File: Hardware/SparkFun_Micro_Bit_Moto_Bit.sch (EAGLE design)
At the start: 47 parts, among them J1 5.5x2.1mm Barrel, J2 CORTEX_DEBUGPTH, J6 1X04_SMD_STRAIGHT_COMBO, U1 CY8C4245LQI-483, U2 TPS62172, U3 micro:bit, U4 DRV8835

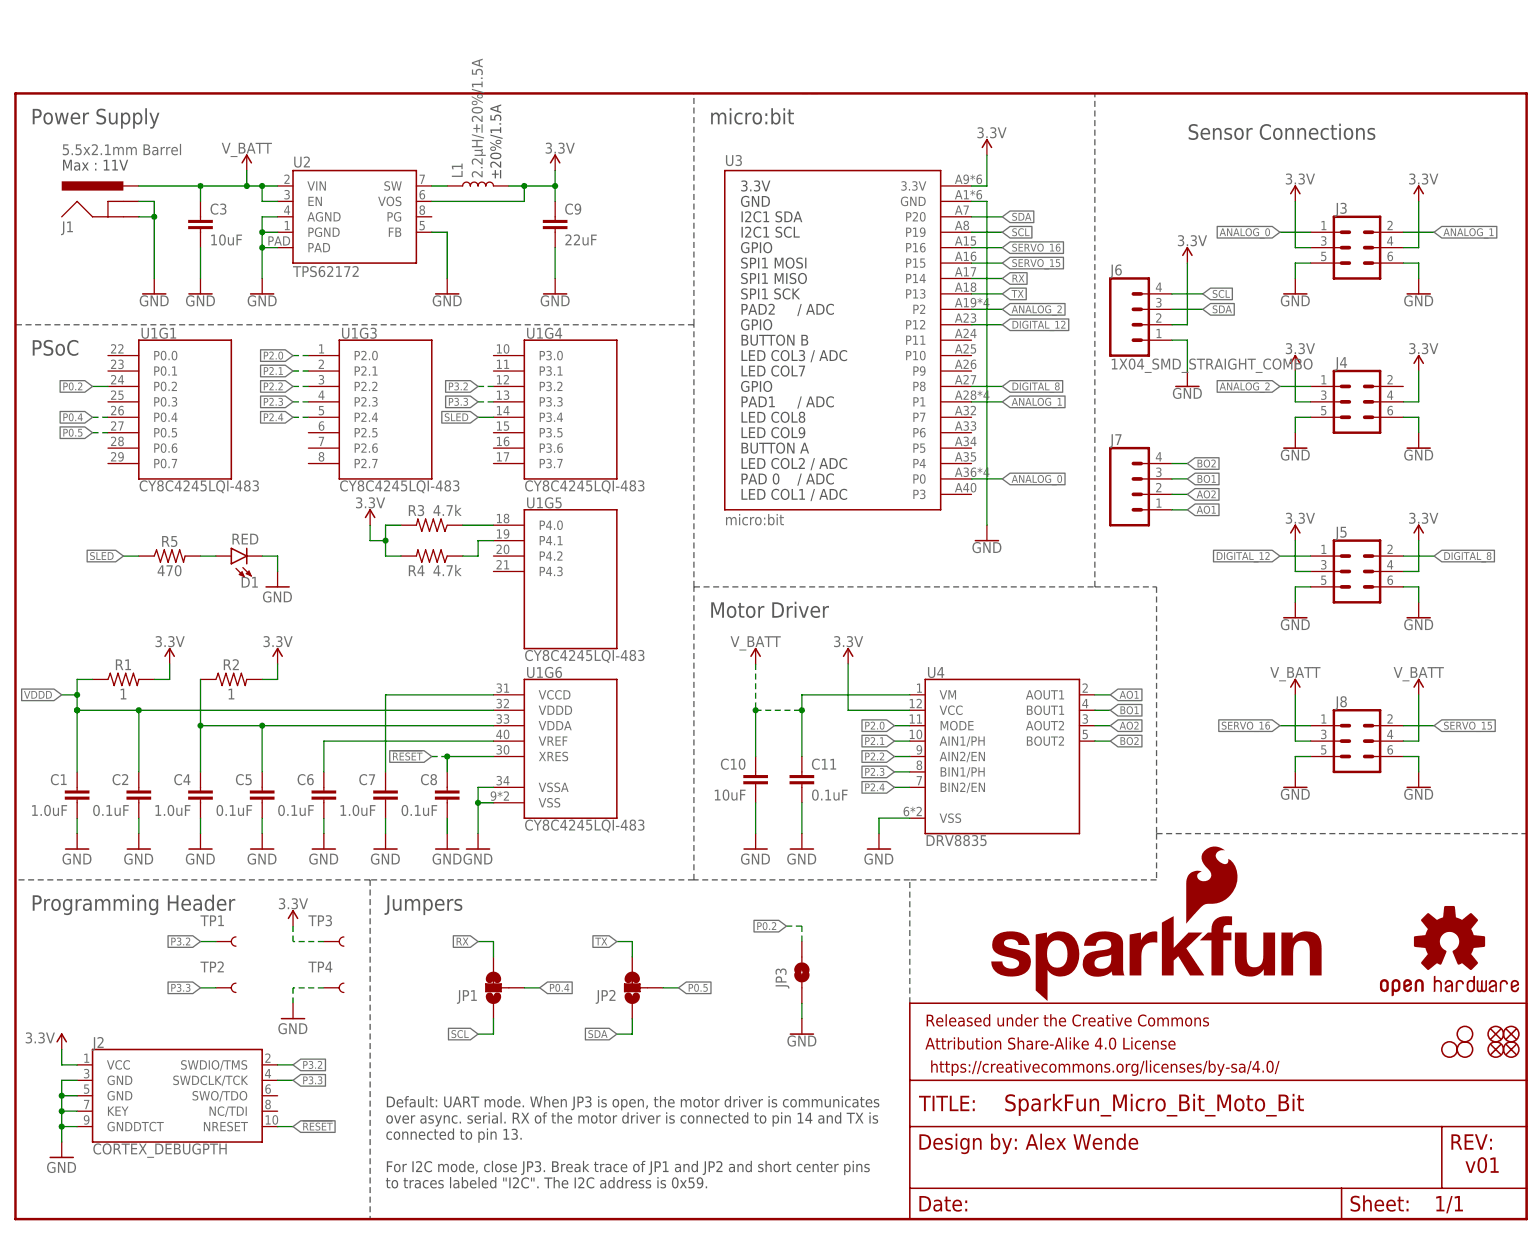
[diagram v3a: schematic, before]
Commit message: Updated Changes
Made a bunch of changes based on suggestions from education
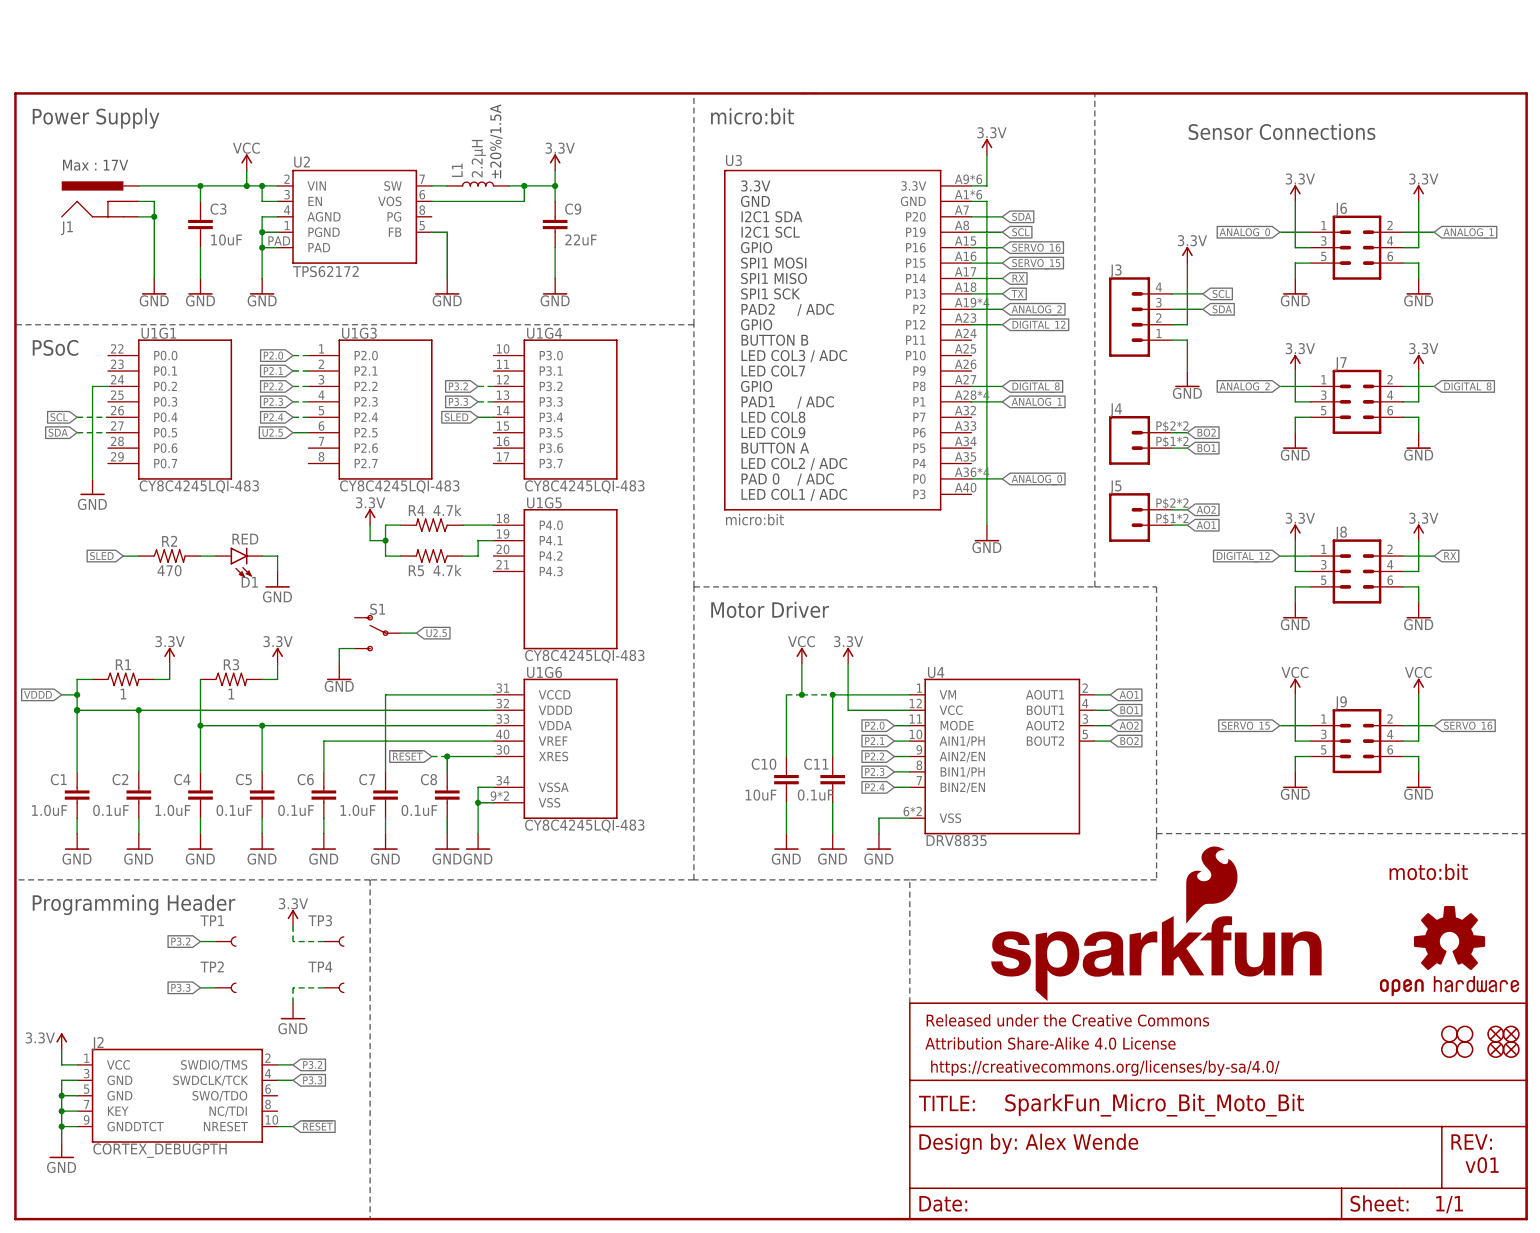
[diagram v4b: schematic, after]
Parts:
- removed JP1, JP2: JUMPER-SMT_3_1-NC_TRACE_SILK, SparkFun-Jumpers:JUMPER-SMT_3_1-NC_TRACE_SILK
- removed JP3: JUMPER-SMT_2_NO_SILK, SparkFun-Jumpers:JUMPER-SMT_2_NO_SILK
- added H1: STAND-OFF, SparkFun-Hardware:STAND-OFF
- added J9: (no value), SparkFun-Connectors:CONN_03X2FEMALE_SMD
- added S1: (no value), SparkFun-Switches:SWITCH-SPDT-PTH-11.6X4.0MM
- added U$3: LOGO-MOTOBIT, Micro_Bit_Parts:LOGO-MOTOBIT
- J1: value 5.5x2.1mm Barrel -> POWER_JACKPTH_LOCK; device SparkFun-Connectors:POWER_JACKSMD -> SparkFun-Connectors:POWER_JACKPTH_LOCK
- J3: device SparkFun-Connectors:CONN_03X2FEMALE_SMD -> SparkFun-Connectors:CONN_04SMD_STRAIGHT_COMBO
- J4, J5: device SparkFun-Connectors:CONN_03X2FEMALE_SMD -> SparkFun-Connectors:CONN_02SMD_RA_FEMALE
- J6: value 1X04_SMD_STRAIGHT_COMBO -> (none); device SparkFun-Connectors:CONN_04SMD_STRAIGHT_COMBO -> SparkFun-Connectors:CONN_03X2FEMALE_SMD
- J7: device SparkFun-Connectors:CONN_04SMD_RA_FEMALE -> SparkFun-Connectors:CONN_03X2FEMALE_SMD
- L1: value 2.2µH/±20%/1.5A -> 2.2µH
- LOGO1: value SFE_LOGO_NAME_FLAME.2_INCH -> SFE_LOGO_NAME_FLAME.3_INCH; device SparkFun-Aesthetics:SFE_LOGO_NAME_FLAME.2_INCH -> SparkFun-Aesthetics:SFE_LOGO_NAME_FLAME.3_INCH
- LOGO2: value OSHW-LOGOM -> OSHW-LOGOL; device SparkFun-Aesthetics:OSHW-LOGOM -> SparkFun-Aesthetics:OSHW-LOGOL
- R2: value 1 -> 470; device SparkFun-Resistors:1OHM-0603-1/10W-1% -> SparkFun-Resistors:470OHM-0603-1/10W-1%
- R3: value 4.7k -> 1; device SparkFun-Resistors:4.7KOHM-0603-1/10W-1% -> SparkFun-Resistors:1OHM-0603-1/10W-1%
- R5: value 470 -> 4.7k; device SparkFun-Resistors:470OHM-0603-1/10W-1% -> SparkFun-Resistors:4.7KOHM-0603-1/10W-1%
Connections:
- removed net P0.2: JP3.2, U1G1.P0.2
- removed net P0.4: JP1.2, U1G1.P0.4
- removed net P0.5: JP2.2, U1G1.P0.5
- removed net V_BATT: C10.1, C11.1, C3.1, J1.PWR, J8.3, J8.4, U2.EN, U2.VIN, U4.VM
- new net U2.5: S1.P, U1G3.P2.5
- new net VCC: C10.1, C11.1, C3.1, J1.PWR, J9.3, J9.4, U2.EN, U2.VIN, U4.VM
- net 3.3V: now also J3.2, J6.3, J6.4, J7.3, J7.4, J8.3, J8.4, R5.2; no longer J3.3, J3.4, J4.3, J4.4, J5.3, J5.4, J6.2, R2.2
- net ANALOG_0: now also J6.1; no longer J3.1
- net ANALOG_1: now also J6.2; no longer J3.2
- net ANALOG_2: now also J7.1; no longer J4.1
- net AO1: now also J5.1; no longer J7.1
- net AO2: now also J5.2; no longer J7.2
- net BO1: now also J4.1; no longer J7.3
- net BO2: now also J4.2; no longer J7.4
- net DIGITAL_12: now also J8.1; no longer J5.1
- net DIGITAL_8: now also J7.2; no longer J5.2
- net GND: now also J3.1, J6.5, J6.6, J7.5, J7.6, J9.5, J9.6, S1.S, U1G1.P0.2; no longer J3.5, J3.6, J4.5, J4.6, J5.5, J5.6, J6.1, JP3.1
- net N$3: now also R3.1; no longer R2.1
- net N$6: now also R4.1; no longer R3.1
- net N$7: now also R5.1; no longer R4.1
- net N$8: now also R2.2; no longer R5.2
- net RX: now also J8.2; no longer JP1.3
- net SCL: now also J3.4, U1G1.P0.4; no longer J6.4, JP1.1
- net SDA: now also J3.3, U1G1.P0.5; no longer J6.3, JP2.1
- net SERVO_15: now also J9.1; no longer J8.2
- net SERVO_16: now also J9.2; no longer J8.1
- net SLED: now also R2.1; no longer R5.1
- net TX: no longer JP2.3
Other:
- note added: "Max : 17V"
- note removed: "Default: UART mode. When JP3 is open, the motor driver is communicates over async. serial. RX of the motor driver is connected to pin 14 and TX is connected to pin 13. For I2C mode, close JP3. Break trace of JP1 and JP2 and short center pins to traces labeled "I2C". The I2C address is 0x59."
- note removed: "Jumpers"
- note removed: "Max : 11V"
- moved on the sheet: C10, C11, J8, R2, R3, R4, R5

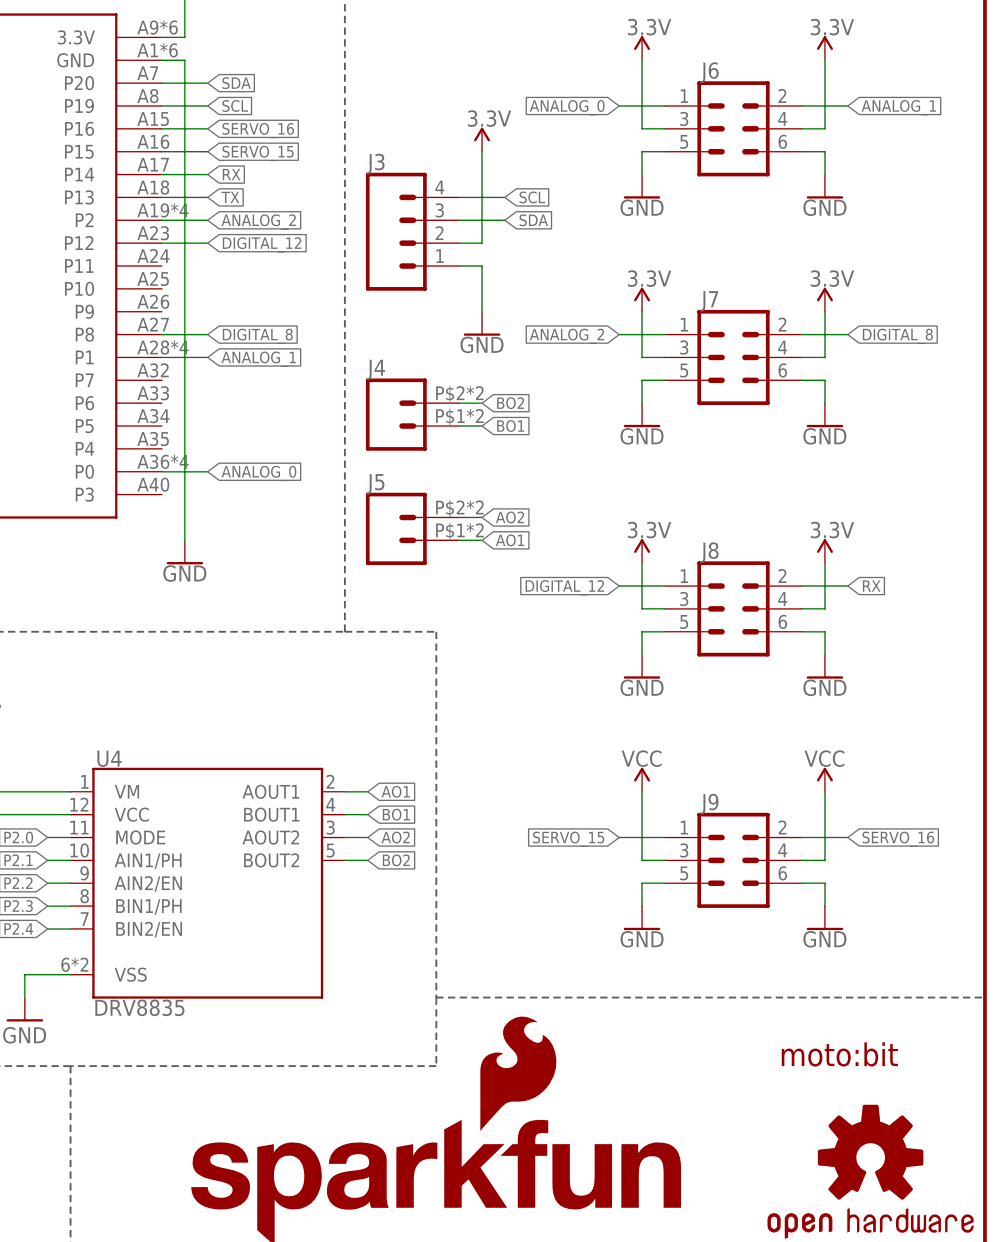
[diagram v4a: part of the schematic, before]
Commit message: Updated Measures Layer
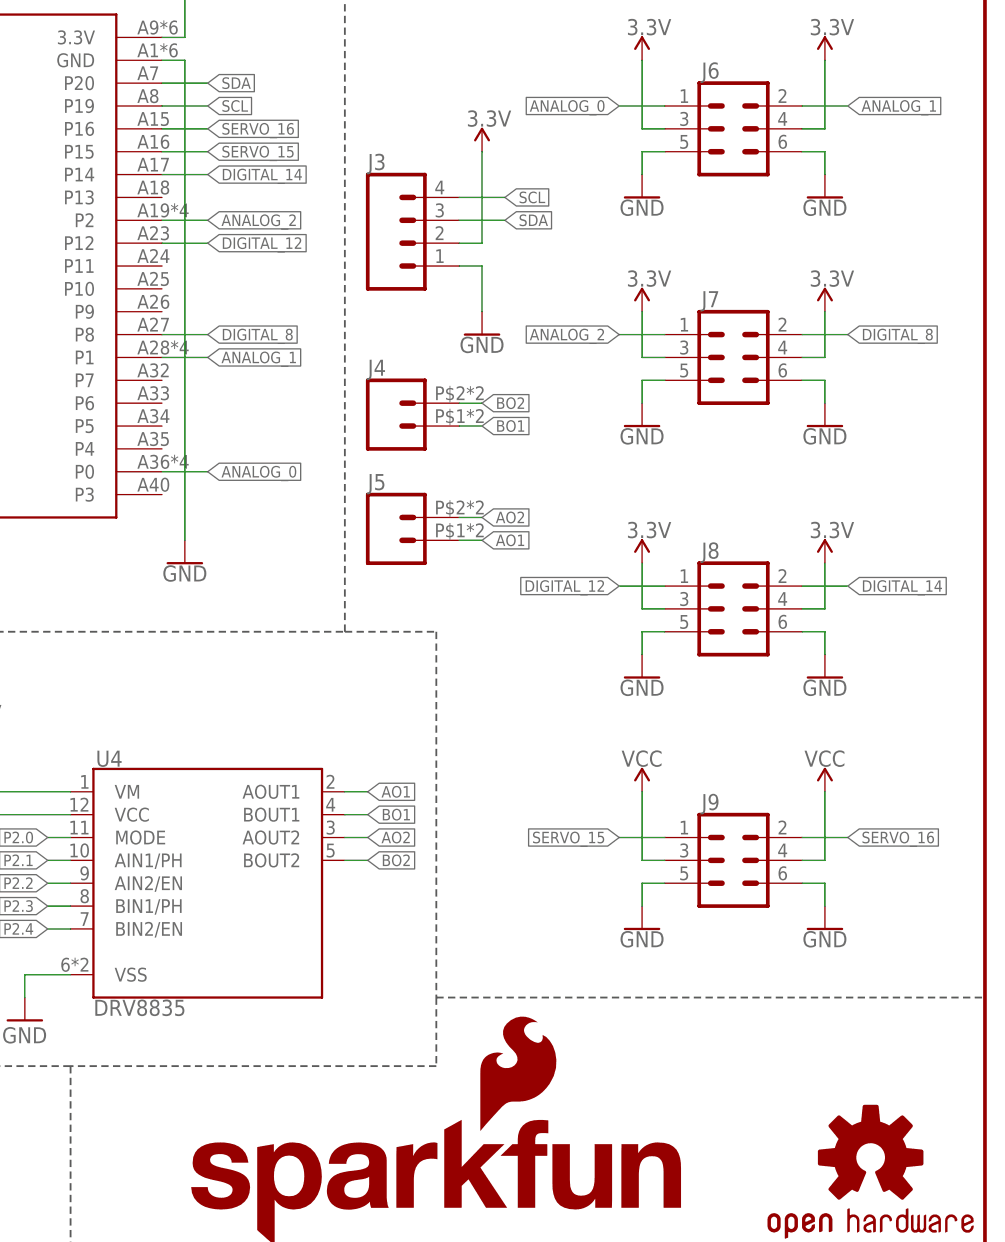
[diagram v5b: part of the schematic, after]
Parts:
- removed U$3: LOGO-MOTOBIT, Micro_Bit_Parts:LOGO-MOTOBIT
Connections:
- net RX renamed DIGITAL_14
- removed net TX: U3.P13
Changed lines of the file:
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@@
 <part name="SUPPLY15" library="SparkFun-PowerSymbols" deviceset="VCC" device=""/>
 <part name="SUPPLY19" library="SparkFun-PowerSymbols" deviceset="VCC" device=""/>
-<part name="U$3" library="Micro_Bit_Parts" deviceset="LOGO-MOTOBIT" device=""/>
 <part name="GND18" library="SparkFun-PowerSymbols" deviceset="GND" device=""/>
 </parts>
@@
 <instance part="SUPPLY15" gate="G$1" x="210.82" y="86.36"/>
 <instance part="SUPPLY19" gate="G$1" x="231.14" y="86.36"/>
-<instance part="U$3" gate="G$1" x="226.06" y="55.88"/>
 <instance part="GND18" gate="1" x="53.34" y="88.9"/>
 </instances>
@@
 </segment>
 </net>
-<net name="RX" class="0">
+<net name="DIGITAL_14" class="0">
 <segment>
 <pinref part="U3" gate="G$1" pin="P14"/>
@@
 </segment>
 </net>
-<net name="TX" class="0">
-<segment>
-<pinref part="U3" gate="G$1" pin="P13"/>
-<wire x1="157.48" y1="152.4" x2="162.56" y2="152.4" width="0.1524" layer="91"/>
-<label x="162.56" y="152.4" size="1.27" layer="95" xref="yes"/>
-</segment>
-</net>

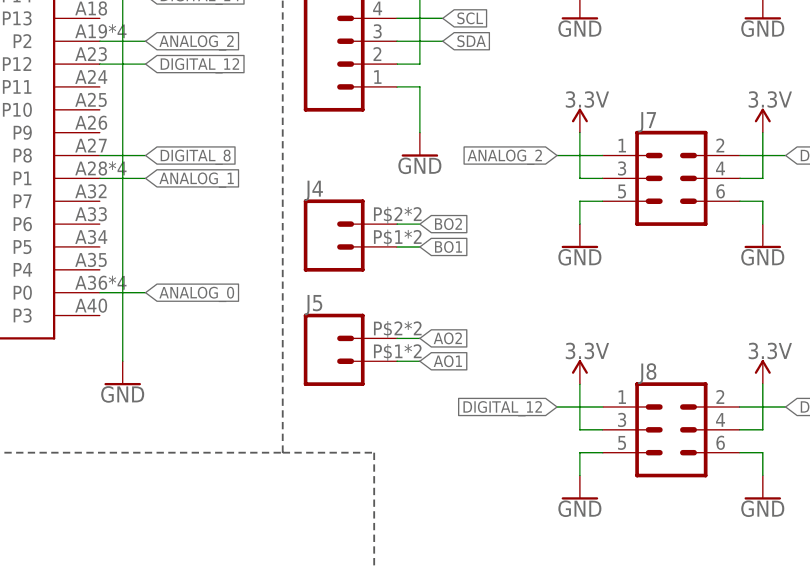
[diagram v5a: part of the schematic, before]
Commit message: Design review changes
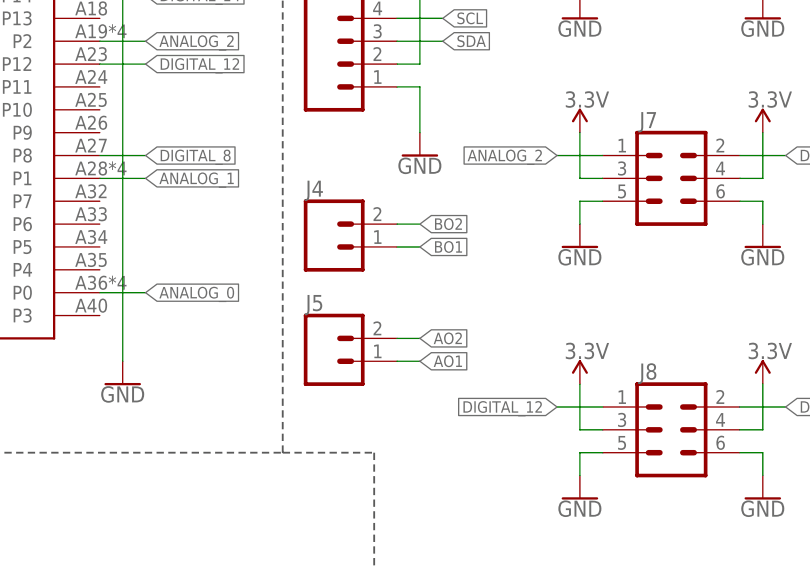
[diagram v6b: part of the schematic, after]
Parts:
- J4, J5: device SparkFun-Connectors:CONN_02SMD_RA_FEMALE -> SparkFun-Connectors:CONN_02PTH_RA_FEMALE
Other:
- moved on the sheet: J4, J5
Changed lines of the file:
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@@
 <part name="GND26" library="SparkFun-PowerSymbols" deviceset="GND" device=""/>
 <part name="GND30" library="SparkFun-PowerSymbols" deviceset="GND" device=""/>
-<part name="J4" library="SparkFun-Connectors" deviceset="CONN_02" device="SMD_RA_FEMALE"/>
-<part name="J5" library="SparkFun-Connectors" deviceset="CONN_02" device="SMD_RA_FEMALE"/>
+<part name="J4" library="SparkFun-Connectors" deviceset="CONN_02" device="PTH_RA_FEMALE"/>
+<part name="J5" library="SparkFun-Connectors" deviceset="CONN_02" device="PTH_RA_FEMALE"/>
 <part name="H1" library="SparkFun-Hardware" deviceset="STAND-OFF" device=""/>
 <part name="SUPPLY3" library="SparkFun-PowerSymbols" deviceset="VCC" device=""/>
